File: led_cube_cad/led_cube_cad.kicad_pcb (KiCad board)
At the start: 2 copper layers, 238.8 x 208.3 mm, 102 parts, among them U1 4099, U2 4099, U3 4099, U4 4099, U5 4099

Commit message: edge cuts
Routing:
- net GND: track 602.1 -> 603.6 mm
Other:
- board size 238.8 x 208.3 mm -> 202.7 x 208.3 mm
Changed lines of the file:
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@@
     (thickness 1.6)
     (drawings 5)
-    (tracks 693)
+    (tracks 694)
     (zones 0)
     (modules 102)
@@
     )
   )
-  (gr_line (start 228.092 -10.16) (end -10.16 -10.16) (layer Edge.Cuts) (width 0.05))
-  (gr_line (start 228.6 198.12) (end 228.092 -10.16) (layer Edge.Cuts) (width 0.05))
-  (gr_line (start -10.16 198.12) (end 228.6 198.12) (layer Edge.Cuts) (width 0.05))
+  (gr_line (start 192.532 -10.16) (end -10.16 -10.16) (layer Edge.Cuts) (width 0.05))
+  (gr_line (start 192.532 198.12) (end 192.532 -10.16) (layer Edge.Cuts) (width 0.05))
+  (gr_line (start -10.16 198.12) (end 192.532 198.12) (layer Edge.Cuts) (width 0.05))
   (gr_line (start -10.16 -10.16) (end -10.16 198.12) (layer Edge.Cuts) (width 0.05))
   (gr_text "+ - A3 A2 A1 D R W1 W2 W3 W4 W5 L1 L2 L3 L4 L5" (at 16.764 114.808 270) (layer F.Cu)
@@
   (segment (start 148.336 153.924) (end 141.154724 153.924) (width 0.75) (layer F.Cu) (net 42))
   (segment (start 157.988 144.272) (end 148.336 153.924) (width 0.75) (layer F.Cu) (net 42))
-  (segment (start 178.308 85.344) (end 178.308 89.408) (width 0.75) (layer F.Cu) (net 42))
-  (segment (start 146.304 53.34) (end 178.308 85.344) (width 0.75) (layer F.Cu) (net 42))
-  (segment (start 146.304 5.588) (end 146.304 53.34) (width 0.75) (layer F.Cu) (net 42))
-  (segment (start 13.716 25.908) (end 13.716 8.636) (width 0.75) (layer F.Cu) (net 42))
-  (segment (start 141.224 0.508) (end 146.304 5.588) (width 0.75) (layer F.Cu) (net 42))
-  (segment (start 16.256 25.908) (end 13.716 25.908) (width 0.75) (layer F.Cu) (net 42))
-  (segment (start 13.716 8.636) (end 21.844 0.508) (width 0.75) (layer F.Cu) (net 42))
-  (segment (start 21.844 0.508) (end 141.224 0.508) (width 0.75) (layer F.Cu) (net 42))
+  (segment (start 13.208 25.908) (end 16.256 25.908) (width 0.75) (layer F.Cu) (net 42))
+  (segment (start 12.192 24.892) (end 13.208 25.908) (width 0.75) (layer F.Cu) (net 42))
+  (segment (start 12.192 10.16) (end 12.192 24.892) (width 0.75) (layer F.Cu) (net 42))
+  (segment (start 21.844 0.508) (end 12.192 10.16) (width 0.75) (layer F.Cu) (net 42))
+  (segment (start 141.224 0.508) (end 21.844 0.508) (width 0.75) (layer F.Cu) (net 42))
+  (segment (start 146.304 5.588) (end 141.224 0.508) (width 0.75) (layer F.Cu) (net 42))
+  (segment (start 146.304 53.34) (end 146.304 5.588) (width 0.75) (layer F.Cu) (net 42))
+  (segment (start 178.308 85.344) (end 146.304 53.34) (width 0.75) (layer F.Cu) (net 42))
+  (segment (start 178.308 89.408) (end 178.308 85.344) (width 0.75) (layer F.Cu) (net 42))
   (segment (start 112.522 143.764) (end 120.396 143.764) (width 0.75) (layer F.Cu) (net 43))
   (segment (start 148.336 115.824) (end 148.336 112.776) (width 0.75) (layer F.Cu) (net 43))

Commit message: trand pads
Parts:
- moved B2Q3 0.51 mm to (90.9, 85.9)
- moved B2Q4 0.51 mm to (90.9, 79.8)
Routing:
- net +5V: track 899.5 -> 947.2 mm
- net Net-(B4Q4-Pad1): track 9.51 -> 11.5 mm
- net Net-(B4Q3-Pad1): track 9.30 -> 11.3 mm
- net Net-(B4Q2-Pad1): track 9.10 -> 11.1 mm
- net Net-(B4Q0-Pad1): track 8.70 -> 10.7 mm
- net Net-(B3Q4-Pad1): track 9.34 -> 11.4 mm
- net Net-(B3Q3-Pad1): track 9.30 -> 11.3 mm
- net Net-(B3Q2-Pad1): track 9.12 -> 11.2 mm
- net Net-(B3Q1-Pad1): track 9.10 -> 11.1 mm
- net Net-(B3Q0-Pad1): track 8.89 -> 10.9 mm
- net Net-(B2Q4-Pad1): track 9.33 -> 11.4 mm
- net Net-(B2Q3-Pad1): track 9.30 -> 11.3 mm
- net Net-(B2Q2-Pad1): track 9.10 -> 11.1 mm
- net Net-(B2Q1-Pad1): track 9.10 -> 11.1 mm
- net Net-(B2Q0-Pad1): track 8.91 -> 10.9 mm
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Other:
- board size 202.7 x 208.3 mm -> 202.7 x 198.6 mm

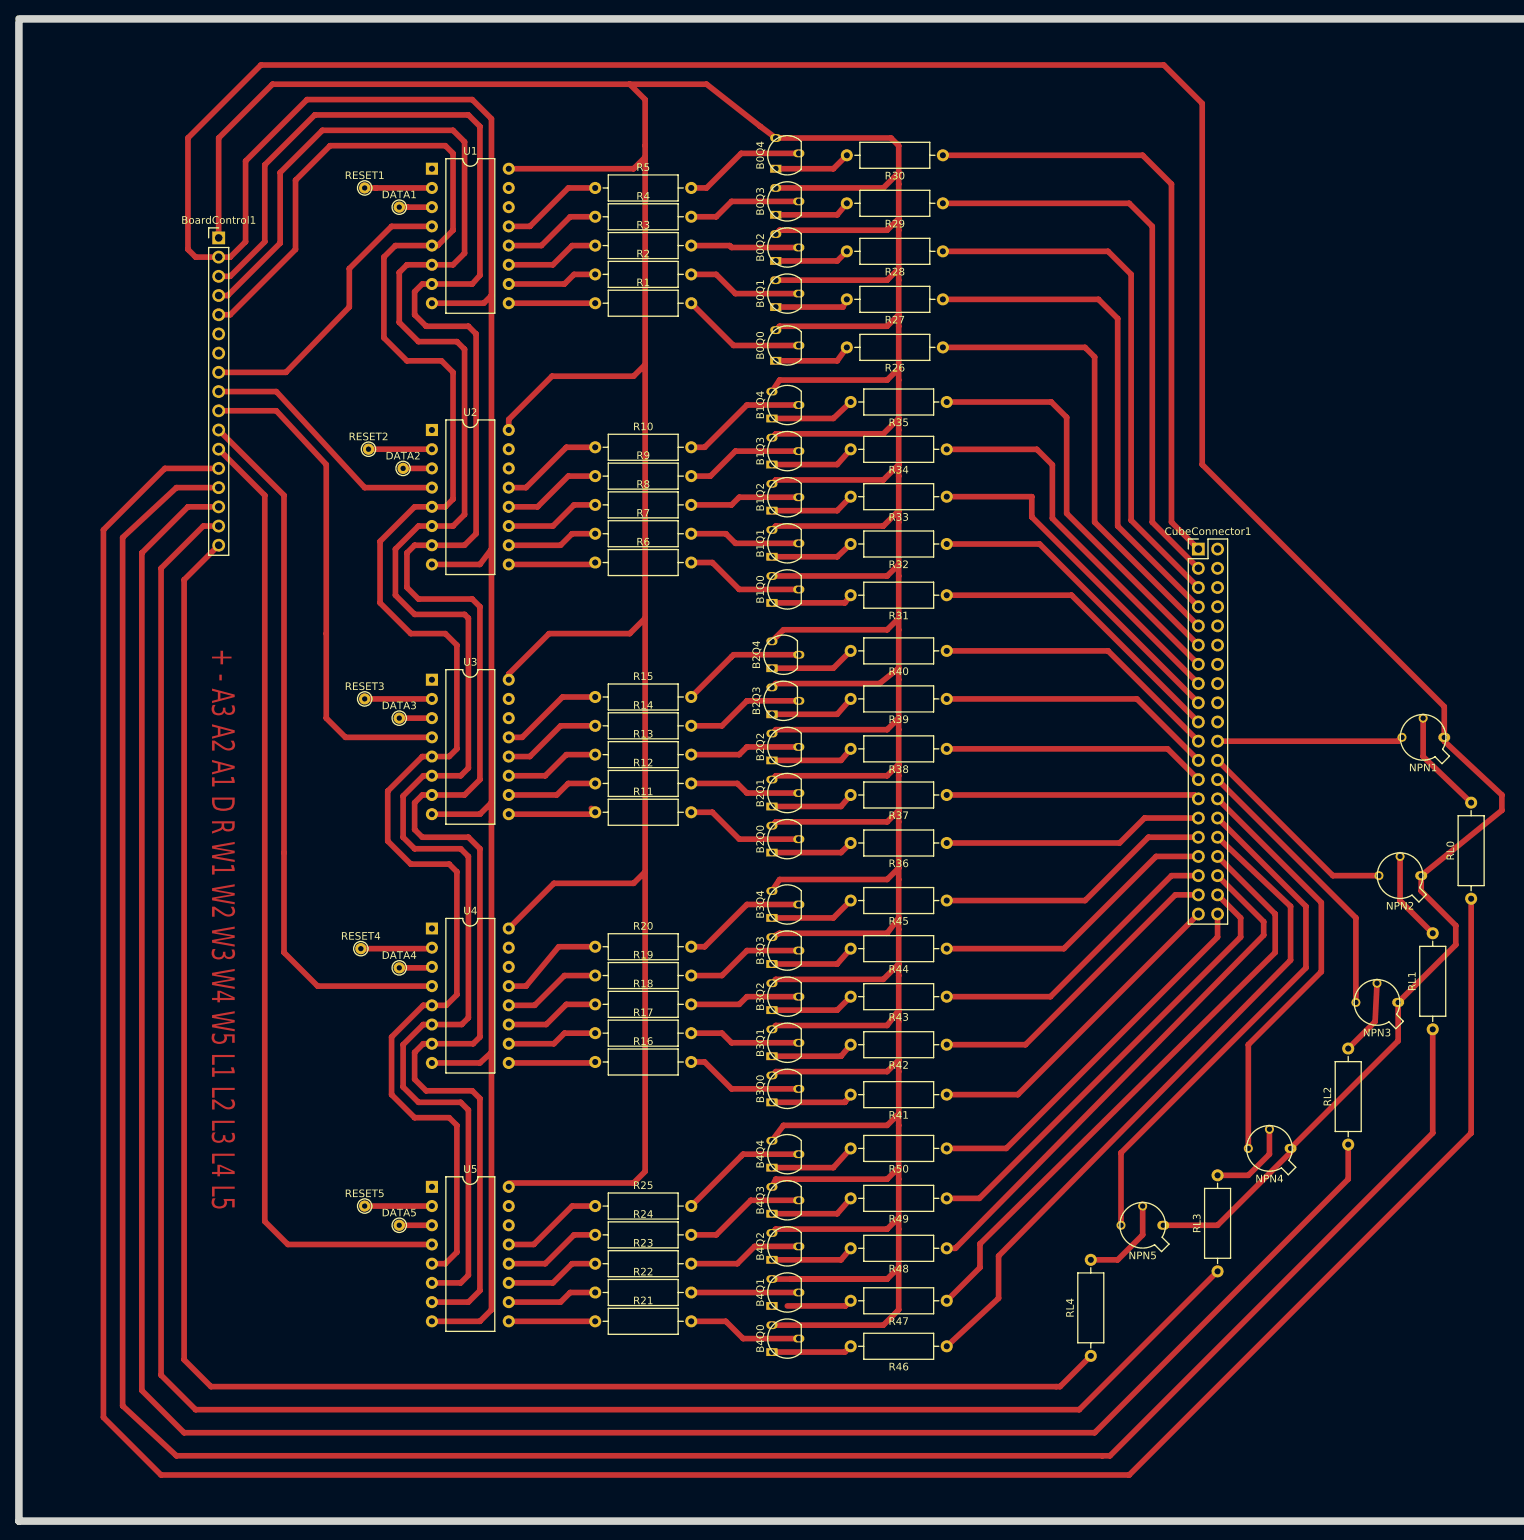
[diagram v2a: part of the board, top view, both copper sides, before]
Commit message: tran pads
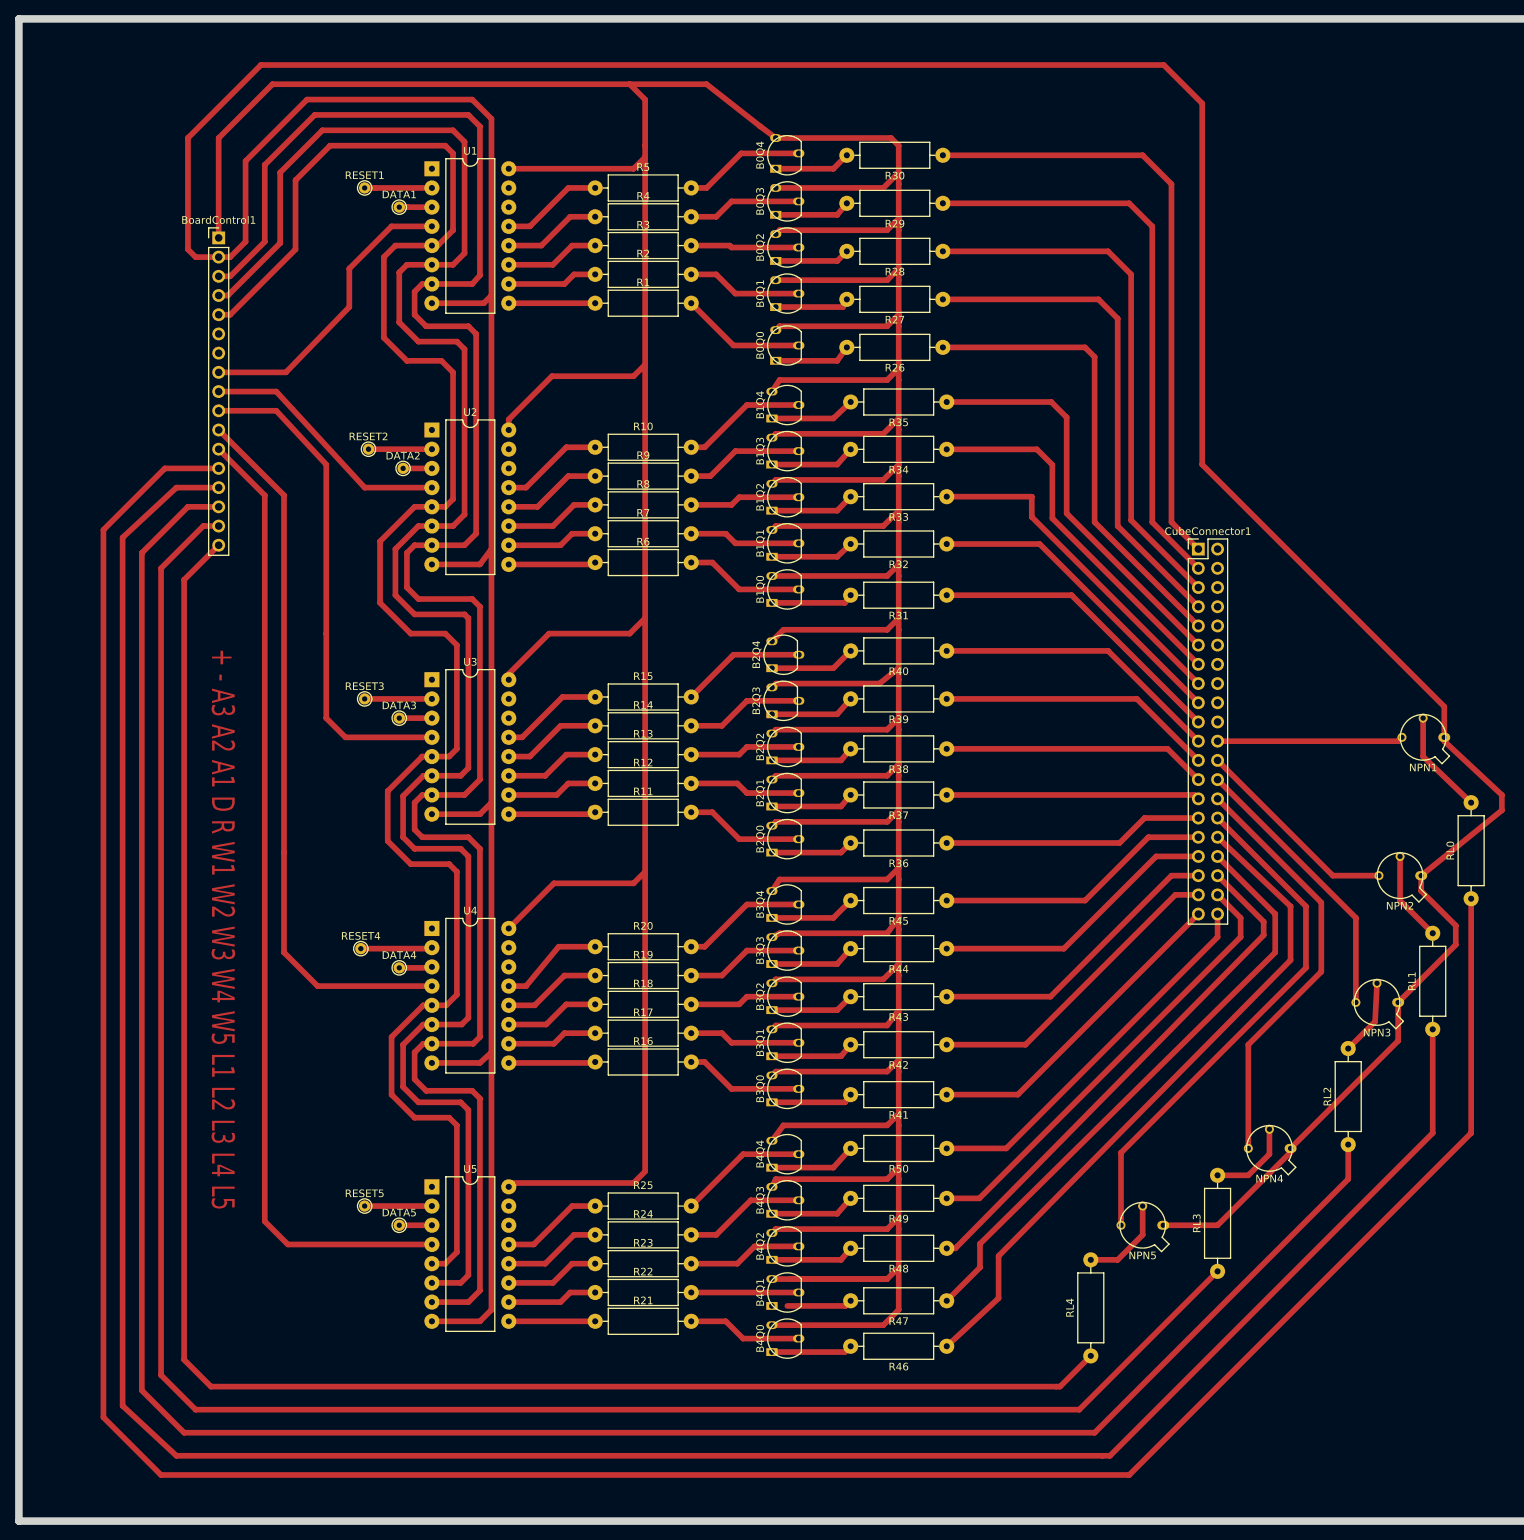
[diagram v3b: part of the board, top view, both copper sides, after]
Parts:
- R1, R10, R11, R12, R13, R14, R15, R16, R17, R18, R19, R2, R20, R21, R22, R23, R24, R25, R26, R27, R28, R29, R3, R30, R31, R32, R33, R34, R35, R36, R37, R38, R39, R4, R40, R41, R42, R43, R44, R45, R46, R47, R48, R49, R5, R50, R6, R7, R8, R9, RL0, RL1, RL2, RL3, RL4: footprint Resistor_THT:R_Axial_DIN0309_L9.0mm_D3.2mm_P12.70mm_Horizontal -> custom-footprints:R_Axial_DIN0309_L9.0mm_D3.2mm_P12.70mm_Horizontal-2mm-pads
- U1, U2, U3, U4, U5: footprint Package_DIP:DIP-16_W10.16mm -> custom-footprints:DIP-16_W10.16mm-2mm-pads
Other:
- outline, holes or cut-outs redrawn

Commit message: fixes and tweaks
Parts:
- B0Q0, B0Q1, B0Q2, B0Q3, B0Q4, B1Q0, B1Q1, B1Q2, B1Q3, B1Q4, B2Q0, B2Q1, B2Q2, B2Q3, B2Q4, B3Q0, B3Q1, B3Q2, B3Q3, B3Q4, B4Q0, B4Q1, B4Q2, B4Q3, B4Q4: footprint Package_TO_SOT_THT:TO-92_Inline -> custom-footprints:TO-92_Inline-2mm-pads
- BoardControl1: footprint Connector_PinHeader_2.54mm:PinHeader_1x17_P2.54mm_Vertical -> custom-footprints:PinHeader_1x17_P2.54mm_Vertical-2mm-pads
- CubeConnector1: footprint Connector_PinHeader_2.54mm:PinHeader_2x20_P2.54mm_Vertical -> custom-footprints:PinHeader_2x20_P2.54mm_Vertical-2mm-pads
- NPN1, NPN2, NPN3, NPN4, NPN5: footprint Package_TO_SOT_THT:TO-18-3 -> custom-footprints:TO-18-3-2mm-pads
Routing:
- net +5V: track 947.2 -> 950.9 mm
- net Net-(B4Q1-Pad1): track 8.91 -> 10.7 mm
- net Net-(B2Q4-Pad2): track 16.5 -> 15.8 mm
- net Net-(B2Q3-Pad2): track 15.6 -> 14.8 mm
- net Net-(B2Q2-Pad1): track 11.1 -> 11.6 mm
- net Net-(B2Q1-Pad2): track 14.8 -> 15.3 mm
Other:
- board text added: "https://github.com/Meyhem/arduino_led_cube"
